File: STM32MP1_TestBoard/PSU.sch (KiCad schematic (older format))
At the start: 25 parts, among them Q1 DMG2302U, U3 TPS54202DDC, U4 TPS54202DDC, U6 STM32G031JxM, U7 MCP603-xCH

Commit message: updated bom, readme
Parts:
- Q1: Mfr (none) -> DiodesInc; PartNo (none) -> DMG2302U
- R12, R13: footprint (none) -> Resistor_SMD:R_0402_1005Metric_Pad0.72x0.64mm_HandSolder
- U6: Mfr (none) -> STMicroelectronics; PartNo (none) -> STM32G031J6M6
- U7: Mfr (none) -> Microchip; PartNo (none) -> MCP603T-E/ST
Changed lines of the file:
@@
 F 2 "Capacitor_SMD:C_0805_2012Metric_Pad1.18x1.45mm_HandSolder" H 5938 1475 50  0001 C CNN
 F 3 "~" H 5900 1625 50  0001 C CNN
+F 4 "~" H 5900 1625 50  0001 C CNN "Mfr"
+F 5 "~" H 5900 1625 50  0001 C CNN "PartNo"
 	1    5900 1625
 	0    1    1    0
@@
 F 2 "Capacitor_SMD:C_0805_2012Metric_Pad1.18x1.45mm_HandSolder" H 7363 2075 50  0001 C CNN
 F 3 "~" H 7325 2225 50  0001 C CNN
+F 4 "~" H 7325 2225 50  0001 C CNN "Mfr"
+F 5 "~" H 7325 2225 50  0001 C CNN "PartNo"
 	1    7325 2225
 	-1   0    0    1
@@
 F 2 "Resistor_SMD:R_0805_2012Metric_Pad1.20x1.40mm_HandSolder" V 7880 2225 50  0001 C CNN
 F 3 "~" H 7950 2225 50  0001 C CNN
+F 4 "~" H 7950 2225 50  0001 C CNN "Mfr"
+F 5 "~" H 7950 2225 50  0001 C CNN "PartNo"
 	1    7950 2225
 	1    0    0    -1
@@
 F 2 "Resistor_SMD:R_0805_2012Metric_Pad1.20x1.40mm_HandSolder" V 7880 2825 50  0001 C CNN
 F 3 "~" H 7950 2825 50  0001 C CNN
+F 4 "~" H 7950 2825 50  0001 C CNN "Mfr"
+F 5 "~" H 7950 2825 50  0001 C CNN "PartNo"
 	1    7950 2825
 	1    0    0    -1
@@
 NoConn ~ 4575 1900
 Wire Wire Line
-	9325 1800 10100 1800
+	9325 1800 9775 1800
 Connection ~ 9325 1800
 $Comp
@@
 F 2 "Capacitor_SMD:C_0805_2012Metric_Pad1.18x1.45mm_HandSolder" H 5938 3825 50  0001 C CNN
 F 3 "~" H 5900 3975 50  0001 C CNN
+F 4 "~" H 5900 3975 50  0001 C CNN "Mfr"
+F 5 "~" H 5900 3975 50  0001 C CNN "PartNo"
 	1    5900 3975
 	0    1    1    0
@@
 F 2 "Capacitor_SMD:C_0805_2012Metric_Pad1.18x1.45mm_HandSolder" H 7363 4425 50  0001 C CNN
 F 3 "~" H 7325 4575 50  0001 C CNN
+F 4 "~" H 7325 4575 50  0001 C CNN "Mfr"
+F 5 "~" H 7325 4575 50  0001 C CNN "PartNo"
 	1    7325 4575
 	-1   0    0    1
@@
 F 2 "Resistor_SMD:R_0805_2012Metric_Pad1.20x1.40mm_HandSolder" V 7880 4575 50  0001 C CNN
 F 3 "~" H 7950 4575 50  0001 C CNN
+F 4 "~" H 7950 4575 50  0001 C CNN "Mfr"
+F 5 "~" H 7950 4575 50  0001 C CNN "PartNo"
 	1    7950 4575
 	1    0    0    -1
@@
 F 2 "Resistor_SMD:R_0805_2012Metric_Pad1.20x1.40mm_HandSolder" V 7880 5175 50  0001 C CNN
 F 3 "~" H 7950 5175 50  0001 C CNN
+F 4 "~" H 7950 5175 50  0001 C CNN "Mfr"
+F 5 "~" H 7950 5175 50  0001 C CNN "PartNo"
 	1    7950 5175
 	1    0    0    -1
@@
 NoConn ~ 4575 4250
 Wire Wire Line
-	9325 4150 10100 4150
+	9325 4150 9775 4150
 Connection ~ 9325 4150
 Text HLabel 10100 4150 2    50   Input ~ 0
@@
 F 2 "Package_TO_SOT_SMD:SOT-23-6" H 12900 7050 50  0001 L CNN
 F 3 "http://ww1.microchip.com/downloads/en/DeviceDoc/21314g.pdf" H 12950 7250 50  0001 C CNN
+F 4 "Microchip" H 12900 7050 50  0001 C CNN "Mfr"
+F 5 "MCP603T-E/ST" H 12900 7050 50  0001 C CNN "PartNo"
 	1    12900 7050
 	1    0    0    -1
@@
 F 1 "DMG2302U" H 13004 8955 50  0000 L CNN
 F 2 "Package_TO_SOT_SMD:SOT-23" H 13000 9100 50  0001 C CNN
-F 3 "~" H 12800 9000 50  0001 C CNN
+F 3 "https://datasheet.octopart.com/DMG2302U-7-Diodes-Inc.-datasheet-103571615.pdf" H 12800 9000 50  0001 C CNN
+F 4 "DiodesInc" H 12800 9000 50  0001 C CNN "Mfr"
+F 5 "DMG2302U" H 12800 9000 50  0001 C CNN "PartNo"
 	1    12800 9000
 	1    0    0    -1
@@
 Wire Wire Line
 	12900 9200 12900 9300
-Wire Wire Line
-	12900 9300 14225 9300
 Text HLabel 14225 9300 2    50   Input ~ 0
 3V3_USB
@@
 F 0 "R12" H 12220 6696 50  0000 L CNN
 F 1 "10K" H 12220 6605 50  0000 L CNN
-F 2 "" V 12080 6650 50  0001 C CNN
+F 2 "Resistor_SMD:R_0402_1005Metric_Pad0.72x0.64mm_HandSolder" V 12080 6650 50  0001 C CNN
 F 3 "~" H 12150 6650 50  0001 C CNN
+F 4 "~" H 12150 6650 50  0001 C CNN "Mfr"
+F 5 "~" H 12150 6650 50  0001 C CNN "PartNo"
 	1    12150 6650
 	1    0    0    -1
@@
 F 0 "R13" H 12220 7271 50  0000 L CNN
 F 1 "10K" H 12220 7180 50  0000 L CNN
-F 2 "" V 12080 7225 50  0001 C CNN
+F 2 "Resistor_SMD:R_0402_1005Metric_Pad0.72x0.64mm_HandSolder" V 12080 7225 50  0001 C CNN
 F 3 "~" H 12150 7225 50  0001 C CNN
+F 4 "~" H 12150 7225 50  0001 C CNN "Mfr"
+F 5 "~" H 12150 7225 50  0001 C CNN "PartNo"
 	1    12150 7225
 	1    0    0    -1
@@
 Wire Wire Line
 	12150 7475 12150 7375
-Wire Wire Line
-	13350 7050 14225 7050
 Connection ~ 13350 7050
 Text HLabel 14225 7050 2    50   Input ~ 0
@@
 F 2 "Package_SO:SO-8_5.3x6.2mm_P1.27mm" H 3600 8750 50  0001 C CNN
 F 3 "https://docs.rs-online.com/1fba/A700000006432306.pdf" H 3600 8750 50  0001 C CNN
+F 4 "STMicroelectronics" H 4450 8750 50  0001 C CNN "Mfr"
+F 5 "STM32G031J6M6" H 4450 8750 50  0001 C CNN "PartNo"
 	1    4450 8750
 	1    0    0    -1
@@
 F 2 "Capacitor_SMD:C_0805_2012Metric_Pad1.18x1.45mm_HandSolder" H 9488 9900 50  0001 C CNN
 F 3 "~" H 9450 10050 50  0001 C CNN
+F 4 "~" H 9450 10050 50  0001 C CNN "Mfr"
+F 5 "~" H 9450 10050 50  0001 C CNN "PartNo"
 	1    9450 10050
 	1    0    0    -1
@@
 F 2 "Capacitor_SMD:C_0805_2012Metric_Pad1.18x1.45mm_HandSolder" H 10013 9900 50  0001 C CNN
 F 3 "~" H 9975 10050 50  0001 C CNN
+F 4 "~" H 9975 10050 50  0001 C CNN "Mfr"
+F 5 "~" H 9975 10050 50  0001 C CNN "PartNo"
 	1    9975 10050
 	1    0    0    -1
@@
 	6150 8550 6150 9900
 Wire Wire Line
-	4100 9800 2775 9800
+	4100 9800 3475 9800
 Wire Wire Line
 	2775 9800 2775 9000
@@
 Connection ~ 2850 1700
 $Comp
-L power:+5V #PWR?
+L power:+5V #PWR0115
 U 1 1 61221242
 P 1675 1250
-F 0 "#PWR?" H 1675 1100 50  0001 C CNN
+F 0 "#PWR0115" H 1675 1100 50  0001 C CNN
 F 1 "+5V" H 1690 1423 50  0000 C CNN
 F 2 "" H 1675 1250 50  0001 C CNN
@@
 Text Notes 1825 1650 0    50   ~ 0
 From USB_Conn.sch
+$Comp
+L power:PWR_FLAG #FLG0101
+U 1 1 6026EA61
+P 9775 1800
+F 0 "#FLG0101" H 9775 1875 50  0001 C CNN
+F 1 "PWR_FLAG" H 9775 1973 50  0000 C CNN
+F 2 "" H 9775 1800 50  0001 C CNN
+F 3 "~" H 9775 1800 50  0001 C CNN
+	1    9775 1800
+	1    0    0    -1
+$EndComp
+Connection ~ 9775 1800
+Wire Wire Line
+	9775 1800 10100 1800
+$Comp
+L power:PWR_FLAG #FLG0102
+U 1 1 60275283
+P 9775 4150
+F 0 "#FLG0102" H 9775 4225 50  0001 C CNN
+F 1 "PWR_FLAG" H 9775 4323 50  0000 C CNN
+F 2 "" H 9775 4150 50  0001 C CNN
+F 3 "~" H 9775 4150 50  0001 C CNN
+	1    9775 4150
+	1    0    0    -1
+$EndComp
+Connection ~ 9775 4150
+Wire Wire Line
+	9775 4150 10100 4150
+Wire Wire Line
+	13350 7050 14225 7050
+$Comp
+L power:PWR_FLAG #FLG0111
+U 1 1 602F578A
+P 3475 9800
+AR Path="/5FBD70AB/602F578A" Ref="#FLG0111"  Part="1"
+AR Path="/6044C48A/602F578A" Ref="#FLG?"  Part="1"
+F 0 "#FLG0111" H 3475 9875 50  0001 C CNN
+F 1 "PWR_FLAG" H 3475 9973 50  0001 C CNN
+F 2 "" H 3475 9800 50  0001 C CNN
+F 3 "~" H 3475 9800 50  0001 C CNN
+	1    3475 9800
+	1    0    0    -1
+$EndComp
+Connection ~ 3475 9800
+Wire Wire Line
+	3475 9800 2775 9800
+Wire Wire Line
+	12900 9300 14225 9300
 $EndSCHEMATC

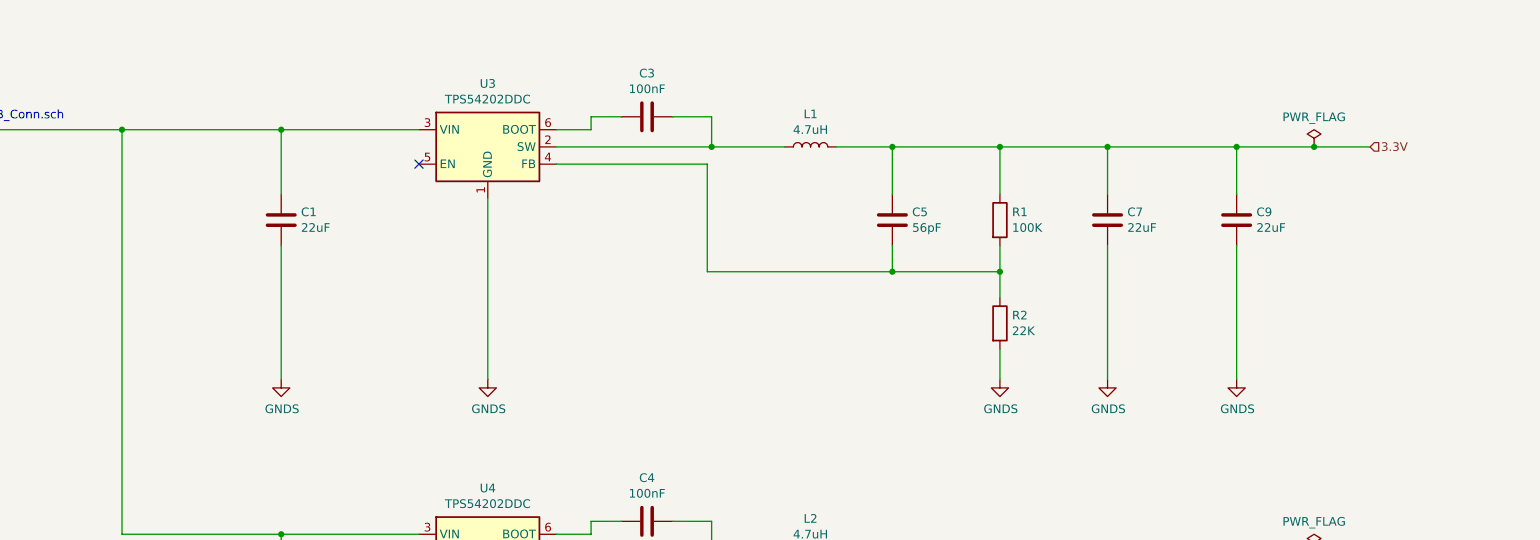
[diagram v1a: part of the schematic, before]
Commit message: swapped smps for ldo
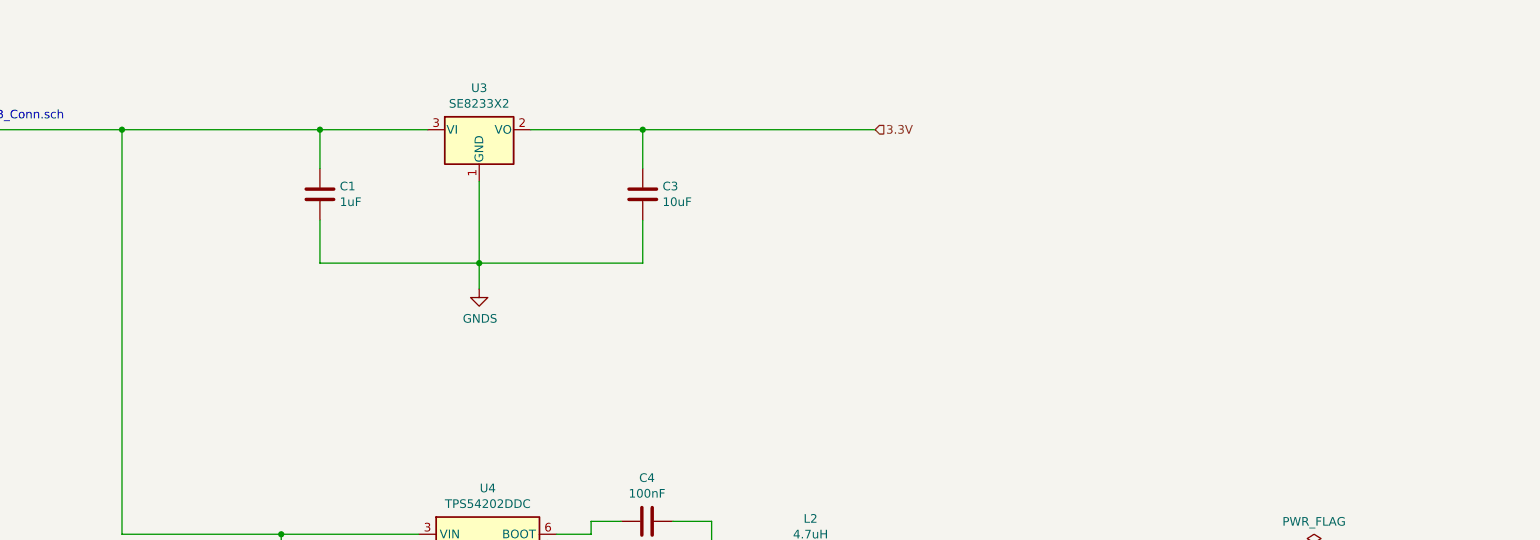
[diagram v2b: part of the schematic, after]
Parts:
- removed C5: 56pF, Capacitor_SMD:C_0805_2012Metric_Pad1.18x1.45mm_HandSolder, symbol Device:C
- removed C7, C9: 22uF, Capacitor_SMD:C_1206_3216Metric_Pad1.33x1.80mm_HandSolder, symbol Device:C
- removed L1: 4.7uH, Inductor_SMD:L_Bourns-SRN6028, symbol Device:L
- removed R1: 100K, Resistor_SMD:R_0805_2012Metric_Pad1.20x1.40mm_HandSolder, symbol Device:R
- removed R2: 22K, Resistor_SMD:R_0805_2012Metric_Pad1.20x1.40mm_HandSolder, symbol Device:R
- removed U3: TPS54202DDC, Package_TO_SOT_SMD:SOT-23-6, symbol Regulator_Switching:TPS54202DDC
- added U3: SE8233X2, Package_TO_SOT_SMD:SOT-23, symbol Regulator_Linear:MCP1700-3302E_SOT23
- C1: value 22uF -> 1uF; footprint Capacitor_SMD:C_1206_3216Metric_Pad1.33x1.80mm_HandSolder -> Capacitor_SMD:C_0402_1005Metric_Pad0.74x0.62mm_HandSolder; Mfr Kemet -> (none); PartNo C1206C226M8PACTU -> (none)
- C3: value 100nF -> 10uF; footprint Capacitor_SMD:C_0805_2012Metric_Pad1.18x1.45mm_HandSolder -> Capacitor_SMD:C_0402_1005Metric_Pad0.74x0.62mm_HandSolder
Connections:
- net +5V: now also U3.3 (VI)
- net 3.3V: now also C3.1, U3.2 (VO)
- net GNDS: now also C3.2, U3.1 (GND)
- no-connect marks 3 -> 2

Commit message: minor schema updates
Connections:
- net 1.35V renamed 1.35V_VDDCORE
- net 3.3V renamed 3.3V_VDD
- net PWR_CTRL_USB_3V3: no longer names the net of U6.6 (PA12[PA10])
- net PWR_CTRL_USB_3V3: no longer Q1.1 (G)
- new net 1V8_DETECT: Q1.1 (G)
- no-connect marks 2 -> 3
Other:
- note added: "to MPU VDD"
- note added: "to MPU VDDCORE"
- moved on the sheet: R12, R13, U7
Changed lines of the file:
@@
 	9325 4150 9775 4150
 Connection ~ 9325 4150
-Text HLabel 10100 4150 2    50   Input ~ 0
-1.35V
+Text HLabel 11550 4150 2    50   Input ~ 0
+1.35V_VDDCORE
 Text HLabel 7225 1700 2    50   Input ~ 0
-3.3V
+3.3V_VDD
 Wire Wire Line
 	2850 1700 2850 4050
@@
 L Amplifier_Operational:MCP603-xCH U7
 U 1 1 603ADBA9
-P 12900 7050
-F 0 "U7" H 13000 7400 50  0000 L CNN
-F 1 "MCP603-xCH" H 12975 7300 50  0000 L CNN
-F 2 "Package_TO_SOT_SMD:SOT-23-6" H 12900 7050 50  0001 L CNN
-F 3 "http://ww1.microchip.com/downloads/en/DeviceDoc/21314g.pdf" H 12950 7250 50  0001 C CNN
-F 4 "Microchip" H 12900 7050 50  0001 C CNN "Mfr"
-F 5 "MCP603T-E/ST" H 12900 7050 50  0001 C CNN "PartNo"
-	1    12900 7050
+P 12625 6400
+F 0 "U7" H 12725 6750 50  0000 L CNN
+F 1 "MCP603-xCH" H 12700 6650 50  0000 L CNN
+F 2 "Package_TO_SOT_SMD:SOT-23-6" H 12625 6400 50  0001 L CNN
+F 3 "http://ww1.microchip.com/downloads/en/DeviceDoc/21314g.pdf" H 12675 6600 50  0001 C CNN
+F 4 "Microchip" H 12625 6400 50  0001 C CNN "Mfr"
+F 5 "MCP603T-E/ST" H 12625 6400 50  0001 C CNN "PartNo"
+	1    12625 6400
 	1    0    0    -1
 $EndComp
@@
 L Device:R R12
 U 1 1 6042E32C
-P 12150 6650
-F 0 "R12" H 12220 6696 50  0000 L CNN
-F 1 "10K" H 12220 6605 50  0000 L CNN
-F 2 "Resistor_SMD:R_0402_1005Metric_Pad0.72x0.64mm_HandSolder" V 12080 6650 50  0001 C CNN
-F 3 "~" H 12150 6650 50  0001 C CNN
-F 4 "~" H 12150 6650 50  0001 C CNN "Mfr"
-F 5 "~" H 12150 6650 50  0001 C CNN "PartNo"
-	1    12150 6650
+P 11875 6000
+F 0 "R12" H 11945 6046 50  0000 L CNN
+F 1 "10K" H 11945 5955 50  0000 L CNN
+F 2 "Resistor_SMD:R_0402_1005Metric_Pad0.72x0.64mm_HandSolder" V 11805 6000 50  0001 C CNN
+F 3 "~" H 11875 6000 50  0001 C CNN
+F 4 "~" H 11875 6000 50  0001 C CNN "Mfr"
+F 5 "~" H 11875 6000 50  0001 C CNN "PartNo"
+	1    11875 6000
 	1    0    0    -1
 $EndComp
@@
 L Device:R R13
 U 1 1 6042EB07
-P 12150 7225
-F 0 "R13" H 12220 7271 50  0000 L CNN
-F 1 "10K" H 12220 7180 50  0000 L CNN
-F 2 "Resistor_SMD:R_0402_1005Metric_Pad0.72x0.64mm_HandSolder" V 12080 7225 50  0001 C CNN
-F 3 "~" H 12150 7225 50  0001 C CNN
-F 4 "~" H 12150 7225 50  0001 C CNN "Mfr"
-F 5 "~" H 12150 7225 50  0001 C CNN "PartNo"
-	1    12150 7225
-	1    0    0    -1
-$EndComp
-Wire Wire Line
-	12600 6950 12150 6950
-Wire Wire Line
-	12150 6800 12150 6950
-Connection ~ 12150 6950
-Wire Wire Line
-	12150 6950 12150 7075
-Wire Wire Line
-	12600 7150 12475 7150
-Wire Wire Line
-	12475 7150 12475 8325
-Wire Wire Line
-	12475 8325 13350 8325
-Wire Wire Line
-	13350 8325 13350 7050
-Wire Wire Line
-	13350 7050 13200 7050
-Wire Wire Line
-	12800 6750 12800 6400
-Wire Wire Line
-	12800 7350 12800 7475
+P 11875 6575
+F 0 "R13" H 11945 6621 50  0000 L CNN
+F 1 "10K" H 11945 6530 50  0000 L CNN
+F 2 "Resistor_SMD:R_0402_1005Metric_Pad0.72x0.64mm_HandSolder" V 11805 6575 50  0001 C CNN
+F 3 "~" H 11875 6575 50  0001 C CNN
+F 4 "~" H 11875 6575 50  0001 C CNN "Mfr"
+F 5 "~" H 11875 6575 50  0001 C CNN "PartNo"
+	1    11875 6575
+	1    0    0    -1
+$EndComp
+Wire Wire Line
+	12325 6300 11875 6300
+Wire Wire Line
+	11875 6150 11875 6300
+Connection ~ 11875 6300
+Wire Wire Line
+	11875 6300 11875 6425
+Wire Wire Line
+	12325 6500 12200 6500
+Wire Wire Line
+	12200 6500 12200 7675
+Wire Wire Line
+	12200 7675 13075 7675
+Wire Wire Line
+	13075 7675 13075 6400
+Wire Wire Line
+	13075 6400 12925 6400
+Wire Wire Line
+	12525 6100 12525 5750
+Wire Wire Line
+	12525 6700 12525 6825
 $Comp
 L power:GNDS #PWR048
 U 1 1 6043AF5B
-P 12800 7475
-F 0 "#PWR048" H 12800 7225 50  0001 C CNN
-F 1 "GNDS" H 12805 7302 50  0000 C CNN
-F 2 "" H 12800 7475 50  0001 C CNN
-F 3 "" H 12800 7475 50  0001 C CNN
-	1    12800 7475
+P 12525 6825
+F 0 "#PWR048" H 12525 6575 50  0001 C CNN
+F 1 "GNDS" H 12530 6652 50  0000 C CNN
+F 2 "" H 12525 6825 50  0001 C CNN
+F 3 "" H 12525 6825 50  0001 C CNN
+	1    12525 6825
 	1    0    0    -1
 $EndComp
@@
 L power:+1V35 #PWR?
 U 1 1 6043B382
-P 12800 6400
+P 12525 5750
 AR Path="/6043B382" Ref="#PWR?"  Part="1"
 AR Path="/6044C48A/6043B382" Ref="#PWR?"  Part="1"
 AR Path="/5FBD70AB/6043B382" Ref="#PWR047"  Part="1"
-F 0 "#PWR047" H 12800 6250 50  0001 C CNN
-F 1 "+1V35" H 12815 6573 50  0000 C CNN
-F 2 "" H 12800 6400 50  0001 C CNN
-F 3 "" H 12800 6400 50  0001 C CNN
-	1    12800 6400
+F 0 "#PWR047" H 12525 5600 50  0001 C CNN
+F 1 "+1V35" H 12540 5923 50  0000 C CNN
+F 2 "" H 12525 5750 50  0001 C CNN
+F 3 "" H 12525 5750 50  0001 C CNN
+	1    12525 5750
 	1    0    0    -1
 $EndComp
@@
 L power:+1V35 #PWR?
 U 1 1 6043BA2E
-P 12150 6400
+P 11875 5750
 AR Path="/6043BA2E" Ref="#PWR?"  Part="1"
 AR Path="/6044C48A/6043BA2E" Ref="#PWR?"  Part="1"
 AR Path="/5FBD70AB/6043BA2E" Ref="#PWR045"  Part="1"
-F 0 "#PWR045" H 12150 6250 50  0001 C CNN
-F 1 "+1V35" H 12165 6573 50  0000 C CNN
-F 2 "" H 12150 6400 50  0001 C CNN
-F 3 "" H 12150 6400 50  0001 C CNN
-	1    12150 6400
-	1    0    0    -1
-$EndComp
-Wire Wire Line
-	12150 6400 12150 6500
+F 0 "#PWR045" H 11875 5600 50  0001 C CNN
+F 1 "+1V35" H 11890 5923 50  0000 C CNN
+F 2 "" H 11875 5750 50  0001 C CNN
+F 3 "" H 11875 5750 50  0001 C CNN
+	1    11875 5750
+	1    0    0    -1
+$EndComp
+Wire Wire Line
+	11875 5750 11875 5850
 $Comp
 L power:GNDS #PWR046
 U 1 1 6043DCF6
-P 12150 7475
-F 0 "#PWR046" H 12150 7225 50  0001 C CNN
-F 1 "GNDS" H 12155 7302 50  0000 C CNN
-F 2 "" H 12150 7475 50  0001 C CNN
-F 3 "" H 12150 7475 50  0001 C CNN
-	1    12150 7475
-	1    0    0    -1
-$EndComp
-Wire Wire Line
-	12150 7475 12150 7375
-Connection ~ 13350 7050
-Text HLabel 14225 7050 2    50   Input ~ 0
+P 11875 6825
+F 0 "#PWR046" H 11875 6575 50  0001 C CNN
+F 1 "GNDS" H 11880 6652 50  0000 C CNN
+F 2 "" H 11875 6825 50  0001 C CNN
+F 3 "" H 11875 6825 50  0001 C CNN
+	1    11875 6825
+	1    0    0    -1
+$EndComp
+Wire Wire Line
+	11875 6825 11875 6725
+Connection ~ 13075 6400
+Text HLabel 13950 6400 2    50   Input ~ 0
 DDR_VREF
 $Comp
@@
 PWR_CTRL_VDDCORE_1V35
 Wire Wire Line
-	5850 8850 6675 8850
-Text Label 6675 8850 0    50   ~ 0
-PWR_CTRL_USB_3V3
-Wire Wire Line
 	5850 9000 6675 9000
 Connection ~ 6075 8700
@@
 Wire Wire Line
 	12600 9000 12075 9000
-Text Label 12075 9000 2    50   ~ 0
-PWR_CTRL_USB_3V3
-Wire Wire Line
-	12900 8000 12075 8000
-Text Label 12075 8000 2    50   ~ 0
+Wire Wire Line
+	12625 7350 11800 7350
+Text Label 11800 7350 2    50   ~ 0
 PWR_CTRL_VDD_REF
 Wire Wire Line
-	12900 8000 12900 7350
+	12625 7350 12625 6700
 $Sheet
 S 4100 9650 900  425
 U 60D82D6A
-F0 "SWD10_Conn1" 50
+F0 "SWD10_Conn1_G031" 50
 F1 "SWD10_Conn.sch" 50
 F2 "SWO" I L 4100 9900 50
@@
 Connection ~ 9775 4150
 Wire Wire Line
-	9775 4150 10100 4150
-Wire Wire Line
-	13350 7050 14225 7050
+	9775 4150 11550 4150
+Wire Wire Line
+	13075 6400 13950 6400
 $Comp
 L power:PWR_FLAG #FLG0111
@@
 Wire Wire Line
 	5875 1700 7225 1700
+Text Notes 6425 1650 0    50   ~ 0
+to MPU VDD
+Text Notes 10350 4075 0    50   ~ 0
+to MPU VDDCORE
+Text HLabel 12075 9000 0    50   Input ~ 0
+1V8_DETECT
+NoConn ~ 5850 8850
 $EndSCHEMATC
